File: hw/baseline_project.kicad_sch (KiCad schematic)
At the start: 22 parts, among them J101 EXT_3V3, Q1 IRLD024PBF, Q101 IRLD024PBF, SW101 UP, SW102 DOWN, SW103 LEFT, U1 HiLetGo_ST7735R, U101 EK-TM4C123GXL, U102 ESP8266-1

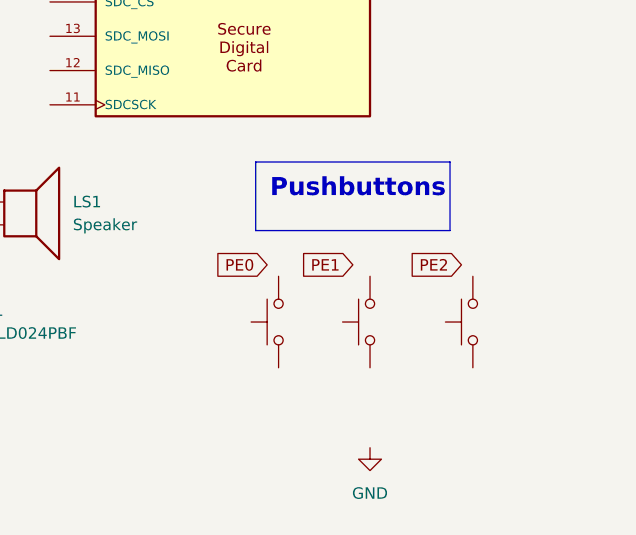
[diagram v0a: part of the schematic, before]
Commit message: LCD digital time test
Co-authored-by: Nav1738 <Nav1738@users.noreply.github.com>
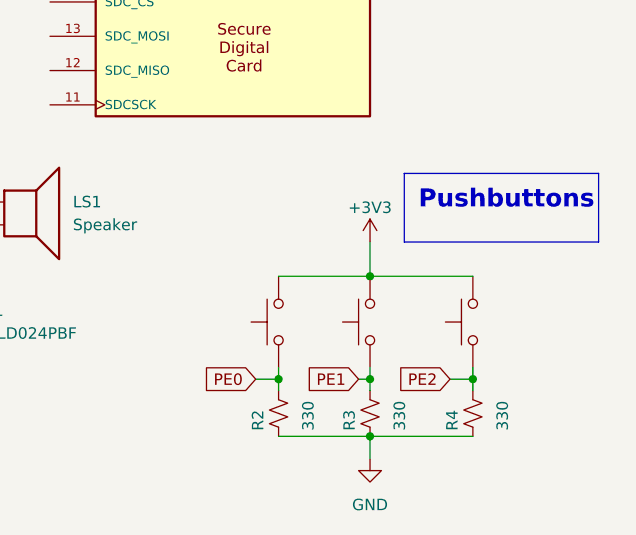
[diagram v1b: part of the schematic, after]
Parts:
- added R2, R3, R4: 330, ECE445L:R_Axial_DIN0204_L3.6mm_D1.6mm_P7.62mm_Horizontal, symbol ECE445L:R_0.125W
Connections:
- net +3V3: now also SW101.2, SW102.2, SW103.2
- net GND: now also R2.1, R3.1, R4.1
- net PE0: now also SW101.1, R2.2
- net PE1: now also SW102.1, R3.2
- net PE2: now also SW103.1, R4.2

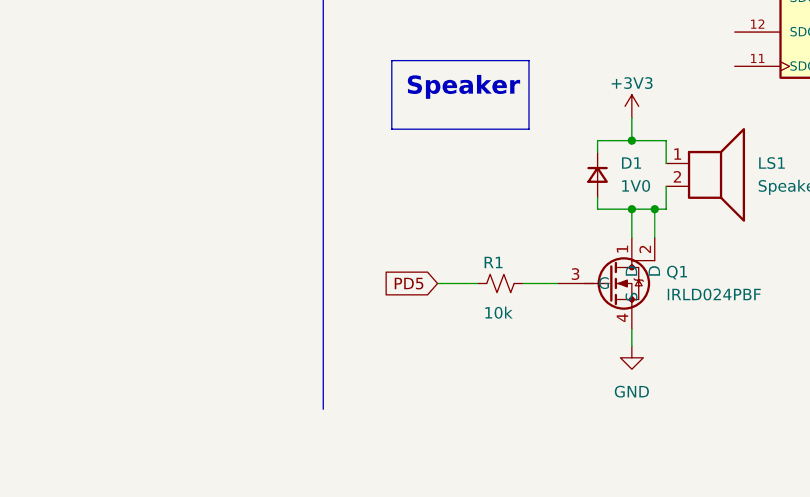
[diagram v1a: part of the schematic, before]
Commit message: Colorscheme & display mode changes are now functional
Co-authored-by: Nav1738 <Nav1738@users.noreply.github.com>
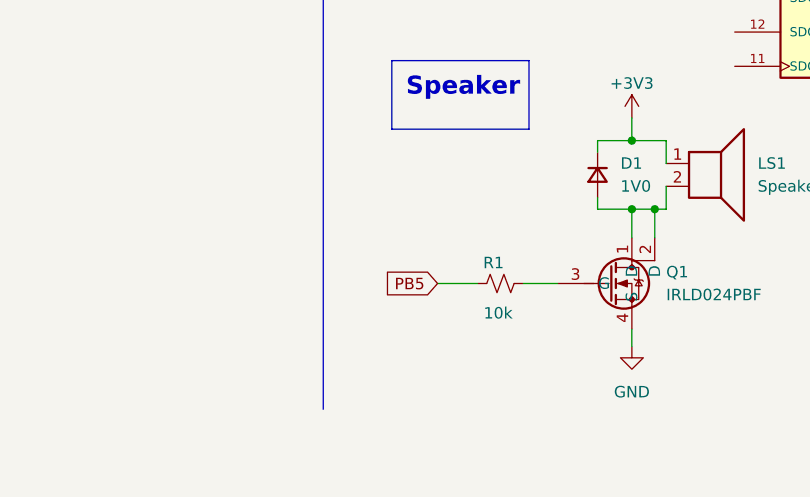
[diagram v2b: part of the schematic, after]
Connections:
- net PD5 is gone; now on net PB5: R1.1
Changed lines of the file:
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@@
 		)
 	)
-	(global_label "PD5"
+	(global_label "PB5"
 		(shape input)
 		(at 189.23 143.51 180)
